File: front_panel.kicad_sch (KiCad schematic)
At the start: 4 parts

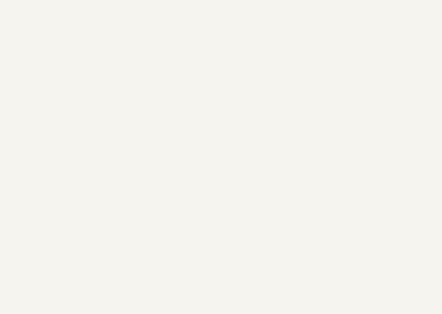
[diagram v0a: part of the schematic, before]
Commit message: Corrected connections for levels and octave switch
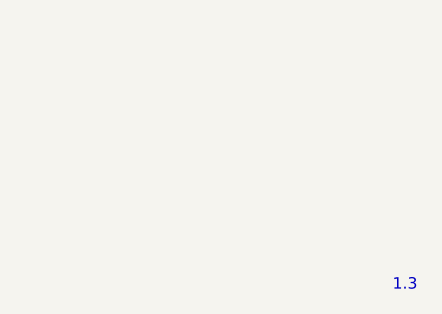
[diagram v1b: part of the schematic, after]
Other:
- note added: "1.3"
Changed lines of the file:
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@@
+		)
+	)
+	(text "1.3"
+		(exclude_from_sim no)
+		(at 183.134 131.318 0)
+		(effects
+			(font
+				(size 1.27 1.27)
+			)
 		)
 	)
